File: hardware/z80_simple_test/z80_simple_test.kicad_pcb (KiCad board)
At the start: 2 copper layers, 95 x 100 mm, 51 parts, among them J1 Barrel_Jack_Switch, J2 Conn_02x15_Odd_Even, U1 Z84C000XPEG, U2 SRAM_512K8B_DIP_SOP_SOJ, U3 EEPROM_512K8B_DIP, U4 74XX138, U5 Z84C40XPEG, U6 74XX32, U7 74XX00

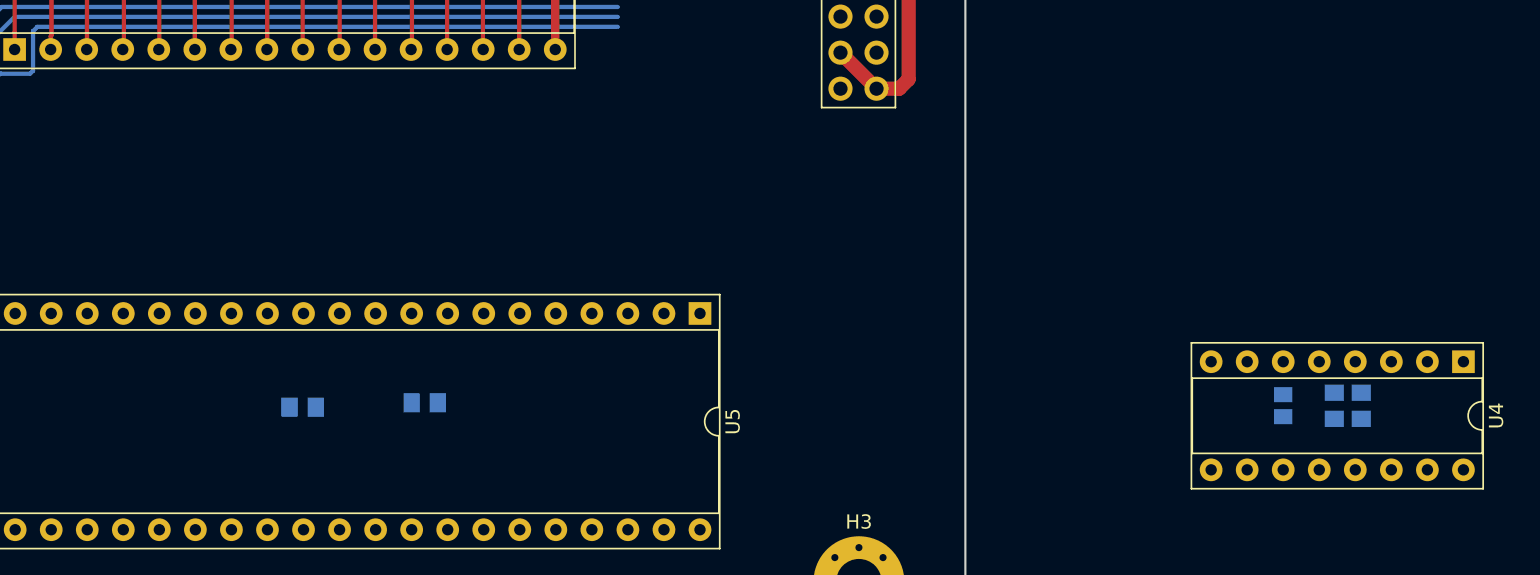
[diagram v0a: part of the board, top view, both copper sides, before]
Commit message: SIO placement
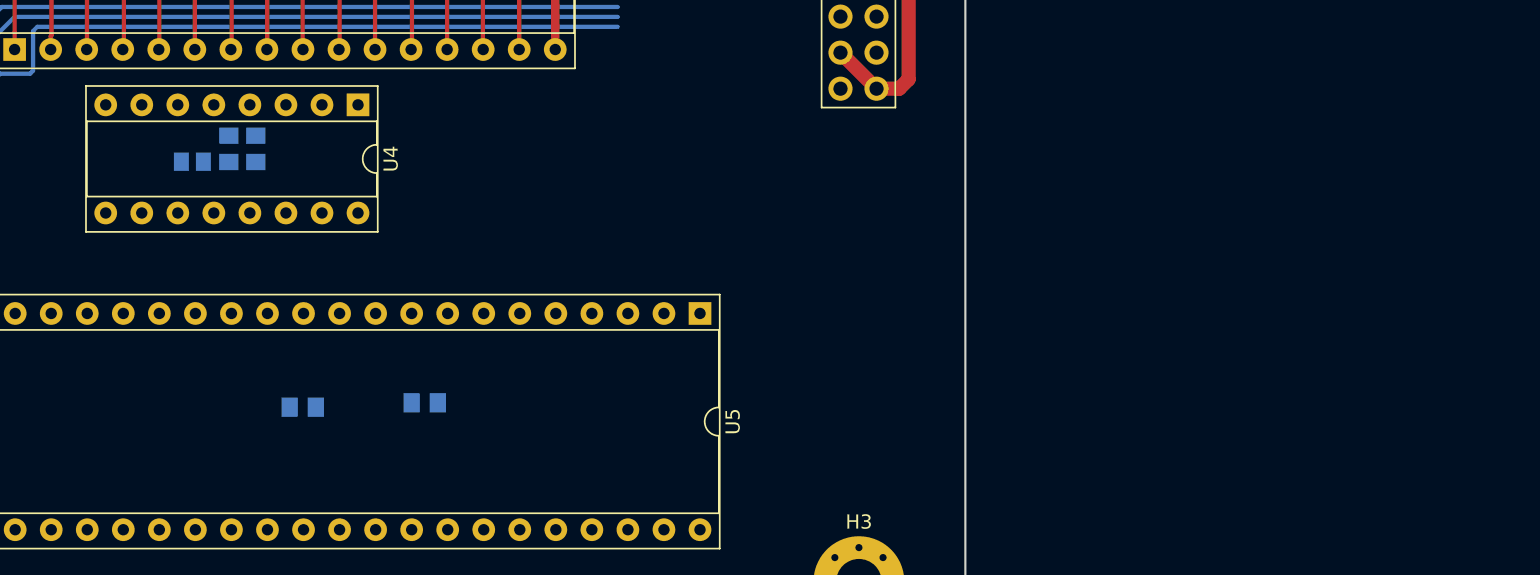
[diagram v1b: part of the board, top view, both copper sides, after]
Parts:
- moved C7 80.0 mm to (145.6, 114.5)
- moved C8 80.0 mm to (147.5, 114.5)
- moved U4 80.0 mm to (154.7, 111.4)
- moved R2 78.8 mm to (143.0, 115.4), turned to 0 degrees
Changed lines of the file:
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@@
   )
   (module SquantorRcl:R_0805+0603 (layer B.Cu)
-    (at 219.9 132.6 270)
+    (at 143.025 115.4)
     (descr "Resistor SMD 0805, reflow soldering, Vishay (see dcrcw.pdf)")
     (tags "resistor 0805")
     (attr smd)
-    (fp_text reference R2 (at 0 2.1 90) (layer B.SilkS)
-      (effects (font (size 1 1) (thickness 0.15)) (justify mirror))
-    )
-    (fp_text value 10k (at 0 -2.1 90) (layer B.Fab)
+    (fp_text reference R2 (at 0 2.1) (layer B.SilkS)
+      (effects (font (size 1 1) (thickness 0.15)) (justify mirror))
+    )
+    (fp_text value 10k (at 0 -2.1) (layer B.Fab)
       (effects (font (size 1 1) (thickness 0.15)) (justify mirror))
     )
@@
     (fp_line (start 1 -0.625) (end -1 -0.625) (layer B.Fab) (width 0.1))
     (fp_line (start -1 -0.625) (end -1 0.625) (layer B.Fab) (width 0.1))
-    (pad 2 smd rect (at 0.775 0 270) (size 1.05 1.3) (layers B.Cu B.Paste B.Mask)
-      (net 2 /VDD))
-    (pad 1 smd rect (at -0.775 0 270) (size 1.05 1.3) (layers B.Cu B.Paste B.Mask)
+    (pad 2 smd rect (at 0.775 0) (size 1.05 1.3) (layers B.Cu B.Paste B.Mask)
+      (net 2 /VDD))
+    (pad 1 smd rect (at -0.775 0) (size 1.05 1.3) (layers B.Cu B.Paste B.Mask)
       (net 38 "Net-(R2-Pad1)"))
     (model ${KISYS3DMOD}/Resistor_SMD.3dshapes/R_0805_2012Metric.step
@@
   )
   (module Package_DIP:DIP-16_W7.62mm_Socket (layer F.Cu)
-    (at 232.6 129.5 270)
+    (at 154.7 111.4 270)
     (descr "16-lead though-hole mounted DIP package, row spacing 7.62 mm (300 mils), Socket")
     (tags "THT DIP DIL PDIP 2.54mm 7.62mm 300mil Socket")
@@
   )
   (module SquantorRcl:C_0805+0603 (layer B.Cu)
-    (at 225.4 132.6 270)
+    (at 147.5 114.5 270)
     (descr "Capacitor SMD 0805 and 0603 pad sizes, reflow soldering, based on AVX dimensions")
     (tags "capacitor 0805 0603 mixed")
@@
   )
   (module SquantorRcl:C_0805+0603 (layer B.Cu)
-    (at 223.5 132.6 270)
+    (at 145.6 114.5 270)
     (descr "Capacitor SMD 0805 and 0603 pad sizes, reflow soldering, based on AVX dimensions")
     (tags "capacitor 0805 0603 mixed")
